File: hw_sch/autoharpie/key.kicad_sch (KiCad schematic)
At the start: 32 parts

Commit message: DAC, touch sensors
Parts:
- renumbered TP5 to TP225, TP9 to TP226, TP17 to TP227, TP25 to TP228, TP1 to TP229, TP2 to TP230, TP10 to TP231, TP11 to TP232, TP18 to TP233, TP19 to TP234, TP26 to TP235, TP27 to TP236, TP6 to TP237, TP12 to TP238, TP20 to TP239, TP28 to TP240, TP3 to TP241, TP13 to TP242, TP21 to TP243, TP29 to TP244, TP4 to TP245, TP7 to TP246, TP14 to TP247, TP15 to TP248, TP22 to TP249, TP23 to TP250, TP30 to TP251, TP31 to TP252, TP8 to TP253, TP16 to TP254, TP24 to TP255, TP32 to TP256
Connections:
- net RX0: now reaches TP225.1
- net RX0: now also TP237.1
- net RX6: now reaches TP243.1
- net RX6: now also TP255.1
- net RX7: now reaches TP256.1
- net RX7: now also TP244.1
- net C0: now reaches TP235.1
- net C0: now also TP229.1, TP230.1, TP231.1, TP232.1, TP233.1, TP234.1, TP236.1, TP245.1, TP246.1, TP247.1, TP248.1, TP249.1, TP250.1, TP251.1, TP252.1
- net RX3: now reaches TP228.1
- net RX3: now also TP240.1
- net RX1: now reaches TP238.1
- net RX1: now also TP226.1
- net RX2: now reaches TP239.1
- net RX2: now also TP227.1
- net RX5: now reaches TP242.1
- net RX5: now also TP254.1
- net RX4: now reaches TP253.1
- net RX4: now also TP241.1
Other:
- moved on the sheet: TP225, TP226, TP227, TP228, TP229, TP230, TP231, TP232, TP233, TP234, TP235, TP236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

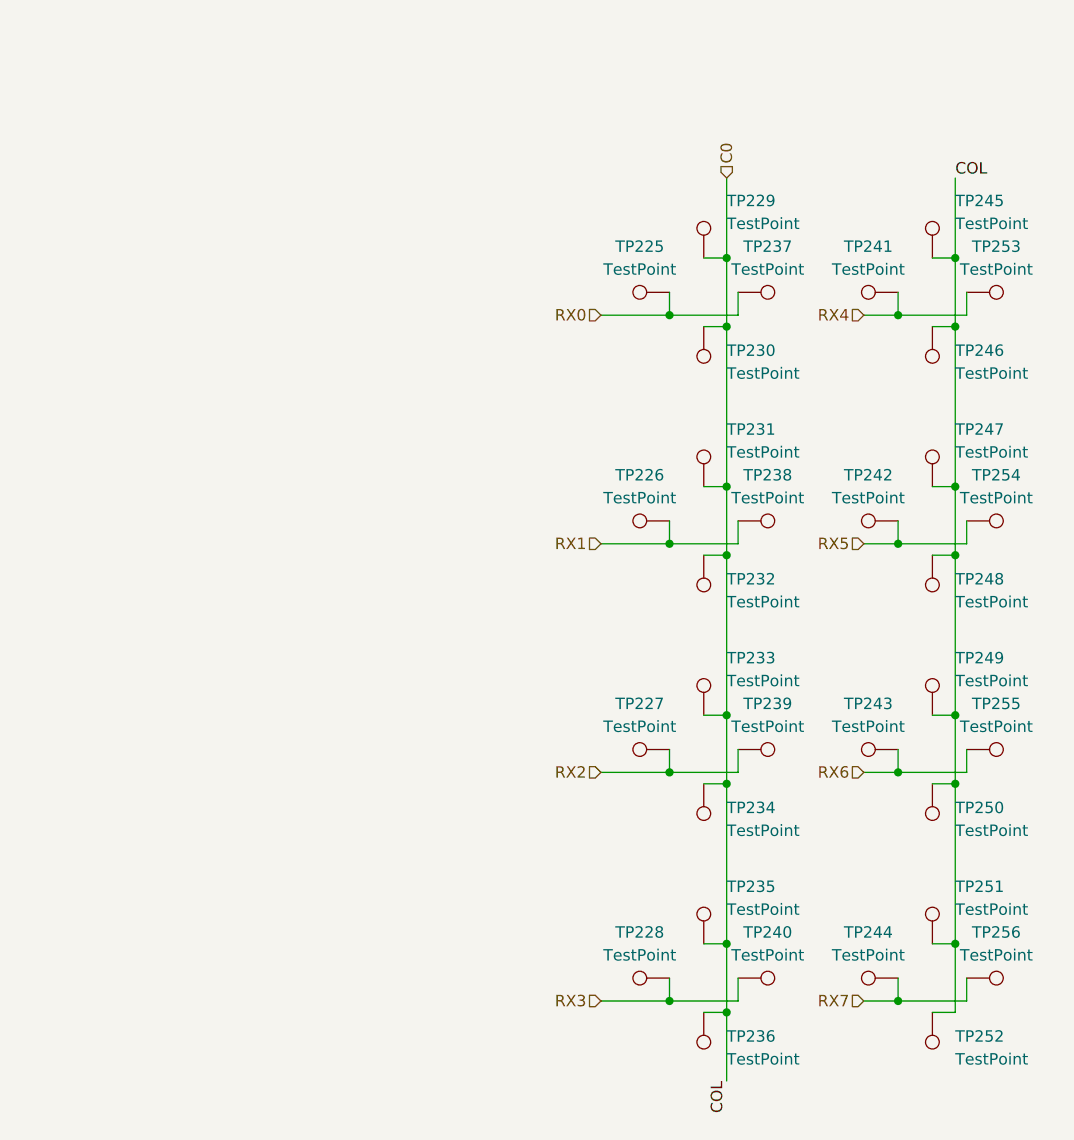
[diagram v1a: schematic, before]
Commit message: seperate keypad
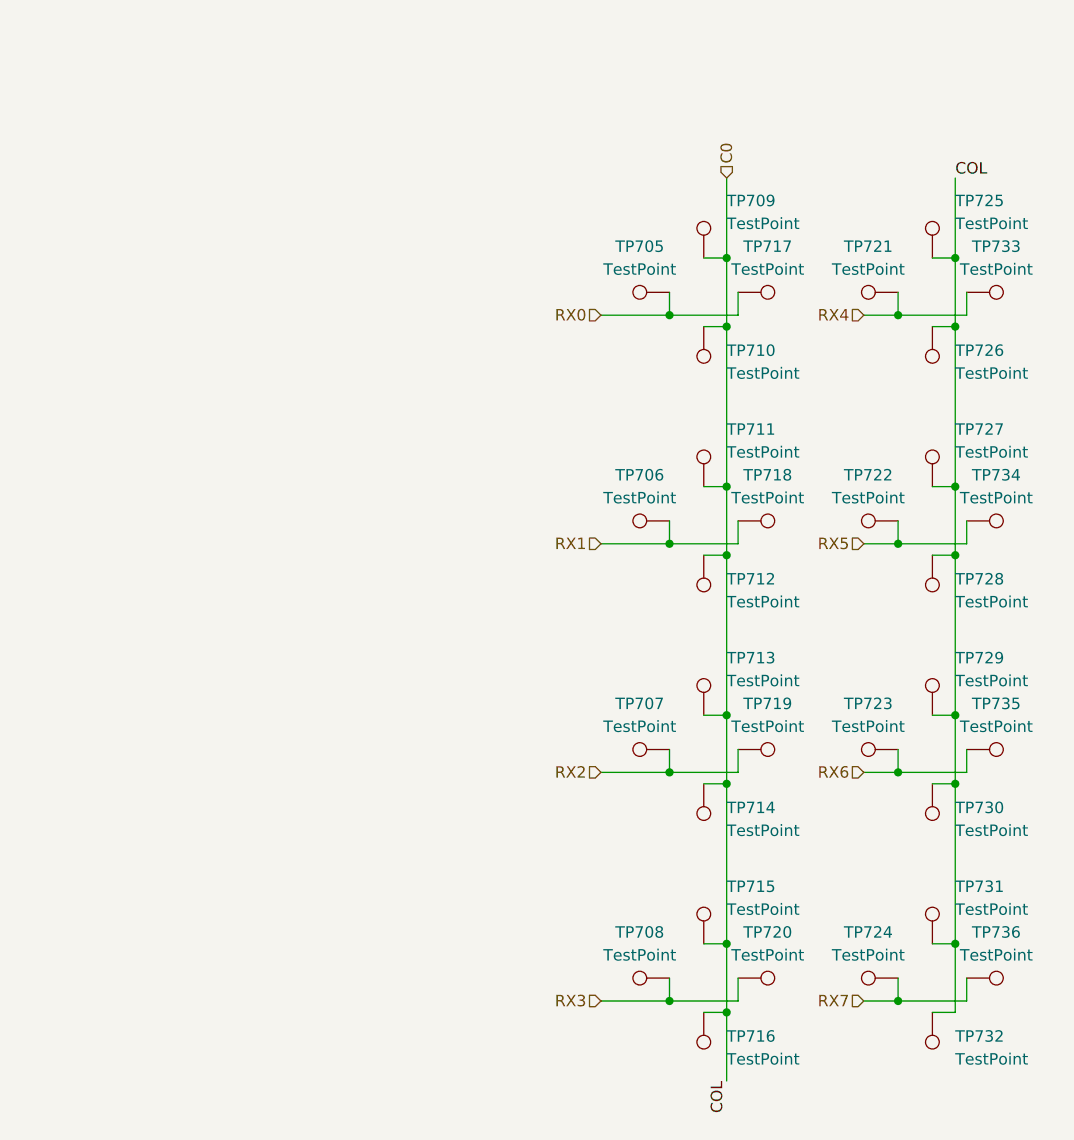
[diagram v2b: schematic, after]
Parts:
- renumbered TP225 to TP705, TP226 to TP706, TP227 to TP707, TP228 to TP708, TP229 to TP709, TP230 to TP710, TP231 to TP711, TP232 to TP712, TP233 to TP713, TP234 to TP714, TP235 to TP715, TP236 to TP716, TP237 to TP717, TP238 to TP718, TP239 to TP719, TP240 to TP720, TP241 to TP721, TP242 to TP722, TP243 to TP723, TP244 to TP724, TP245 to TP725, TP246 to TP726, TP247 to TP727, TP248 to TP728, TP249 to TP729, TP250 to TP730, TP251 to TP731, TP252 to TP732, TP253 to TP733, TP254 to TP734, TP255 to TP735, TP256 to TP736
